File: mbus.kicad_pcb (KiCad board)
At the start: 2 copper layers, 62.9 x 27.2 mm, 37 parts, among them J1 USB_C_Receptacle_USB2.0, J2 MBUS, Q1 BC817, Q2 BC817, Q3 BC807, U1 AP3015, U2 USBLC6-2SC6, U3 CH340E

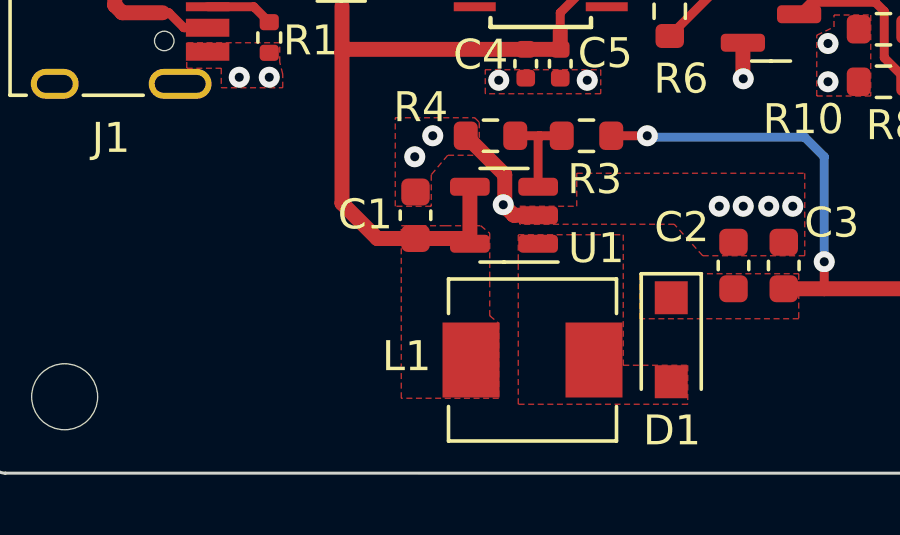
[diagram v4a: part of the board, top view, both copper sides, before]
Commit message: Added CH340N symbol just in case, added part numbers for the rest of the passive components
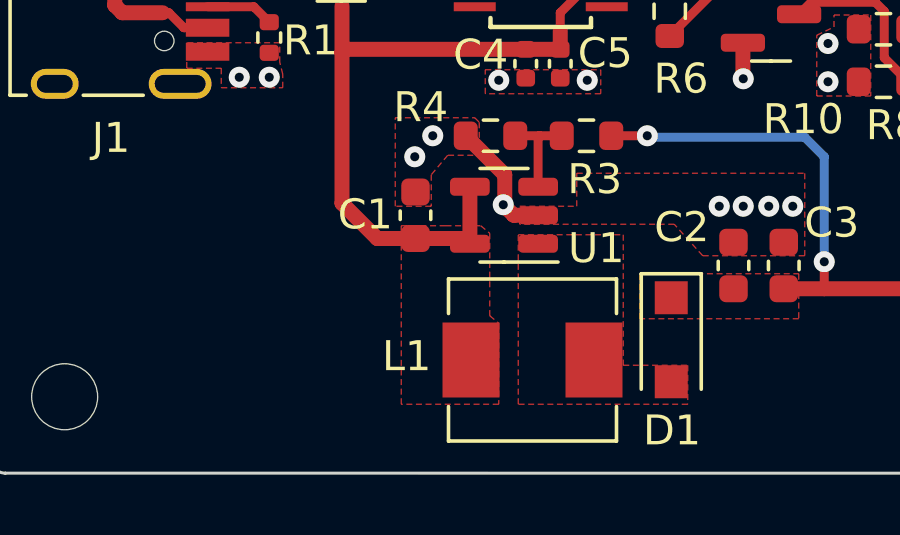
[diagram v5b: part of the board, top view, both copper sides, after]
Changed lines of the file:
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@@
         (xy 59.95 88.55)
         (xy 60.25 88.8)
-        (xy 60.25 91.3)
-        (xy 57 91.3)
+        (xy 60.25 91.5)
+        (xy 57 91.5)
         (xy 57 85.55)
         (xy 58.475 85.55)
